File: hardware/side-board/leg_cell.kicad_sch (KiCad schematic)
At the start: 63 parts, among them IC201 STM32C092KCT6, IC202 TCAN332DR, IC203 TPS56A37RPAR, IC204 INA181A1IDBVR, J201 Servo Connector, J202 Servo Connector, J203 Servo Connector, J204 TC2050, J205 Conn_01x06

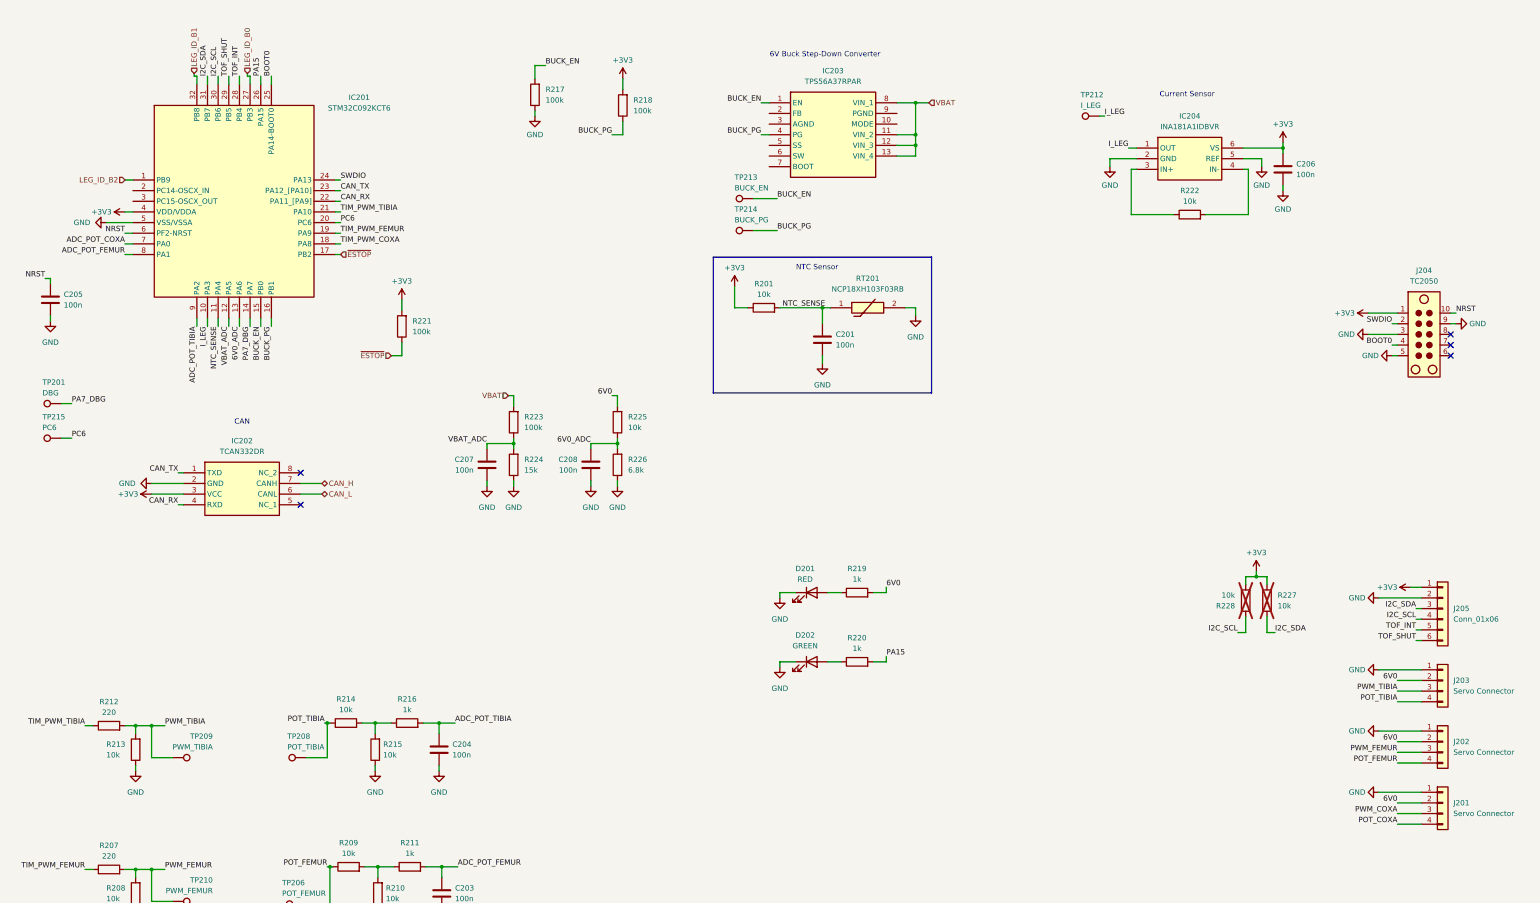
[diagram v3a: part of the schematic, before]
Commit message: Updated schematic for leg
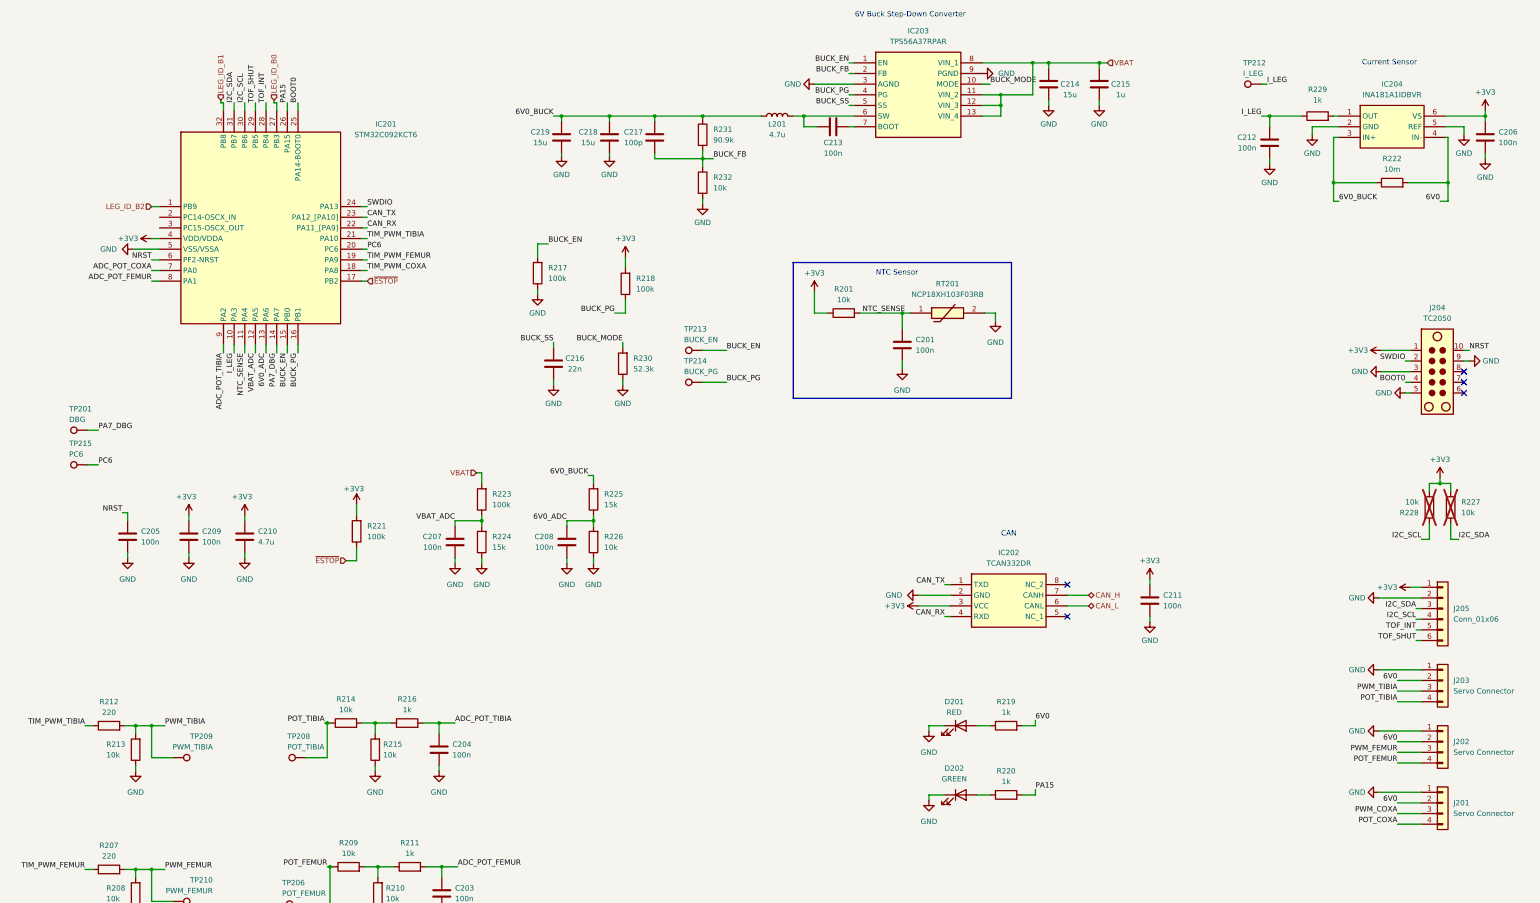
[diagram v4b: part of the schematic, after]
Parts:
- added C209, C211, C212, C213: 100n, Capacitor_SMD:C_0805_2012Metric, symbol Device:C
- added C210: 4.7u, Capacitor_SMD:C_0805_2012Metric, symbol Device:C
- added C214, C218, C219: 15u, Capacitor_SMD:C_0805_2012Metric, symbol Device:C
- added C215: 1u, Capacitor_SMD:C_0805_2012Metric, symbol Device:C
- added C216: 22n, Capacitor_SMD:C_0805_2012Metric, symbol Device:C
- added C217: 100p, Capacitor_SMD:C_0805_2012Metric, symbol Device:C
- added L201: 4.7u, symbol Device:L
- added R229: 1k, Resistor_SMD:R_0603_1608Metric, symbol Device:R
- added R230: 52.3k, Resistor_SMD:R_0603_1608Metric, symbol Device:R
- added R231: 90.9k, Resistor_SMD:R_0805_2012Metric, symbol Device:R
- added R232: 10k, Resistor_SMD:R_0805_2012Metric, symbol Device:R
- R222: value 10k -> 10m; footprint Resistor_SMD:R_0603_1608Metric -> Resistor_SMD:R_2512_6332Metric
- R225: value 10k -> 15k
- R226: value 6.8k -> 10k
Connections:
- net +3V3: now also C209.2, C210.2, C211.2
- net 6V0: now also IC204.4 (IN-), R222.2; no longer R225.2
- net GND: now also IC203.3 (AGND), IC203.9 (PGND), C209.1, C210.1, C211.1, C212.2, C214.2, C215.2, C216.2, C218.1, C219.1, R230.1, R232.2
- net I_LEG: now also C212.1, R229.1; no longer IC204.1 (OUT)
- net VBAT: now also C214.1, C215.1
- net 6V0_BUCK: now reaches IC204.3 (IN+), R222.1
- net 6V0_BUCK: now also R225.2, C217.2, C218.2, C219.2, L201.1, R231.1
- net BUCK_MODE: now reaches IC203.10 (MODE)
- net BUCK_MODE: now also R230.2
- net BUCK_FB: now reaches IC203.2 (FB)
- net BUCK_FB: now also C217.1, R231.2, R232.1
- net BUCK_SS: now reaches IC203.5 (SS)
- net BUCK_SS: now also C216.1
- net at IC203.6 (SW): now also C213.2, L201.2
- net at IC203.7 (BOOT): now also C213.1
- new net: IC204.1 (OUT), R229.2
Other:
- moved on the sheet: C201, C205, C206, C207, C208, D201, D202, IC201, IC202, IC203, IC204, J204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

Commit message: Updated side board schematic
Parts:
- added C220, C221: 10p, Capacitor_SMD:C_0805_2012Metric, symbol Device:C
- added Y201: Crystal_GND24, Crystal:Crystal_SMD_2016-4Pin_2.0x1.6mm, symbol Device:Crystal_GND24
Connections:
- net GND: now also C220.1, C221.1, Y201.2 (G), Y201.4 (G)
- net OSC_IN: now reaches IC201.2 (PC14-OSCX_IN)
- net OSC_IN: now also C221.2, Y201.3
- net OSC_OUT: now reaches IC201.3 (PC15-OSCX_OUT)
- net OSC_OUT: now also C220.2, Y201.1
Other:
- note added: "Configs"
- moved on the sheet: C201, C205, C206, C207, C208, C209, C210, C212, C213, C214, C215, C216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

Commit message: Segregated specific libs into shared libs
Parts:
- IC201: footprint side-board:QFP80P900X900X160-32N -> vector:QFP80P900X900X160-32N; symbol side-board:STM32C092KCT6 -> vector:STM32C092KCT6
- IC202: footprint side-board:SOIC127P600X175-8N -> vector:SOIC127P600X175-8N; symbol side-board:TCAN332DR -> vector:TCAN332DR
- RT201: footprint side-board:THRMC1608X95N -> vector:THRMC1608X95N; symbol side-board:NCP18XH103F03RB -> vector:NCP18XH103F03RB
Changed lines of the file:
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@@
 	)
 	(symbol
-		(lib_id "side-board:TCAN332DR")
+		(lib_id "vector:TCAN332DR")
 		(at 244.475 154.94 0)
 		(unit 1)
@@
 			)
 		)
-		(property "Footprint" "side-board:SOIC127P600X175-8N"
+		(property "Footprint" "vector:SOIC127P600X175-8N"
 			(at 268.605 249.86 0)
 			(hide yes)
@@
 	)
 	(symbol
-		(lib_id "side-board:NCP18XH103F03RB")
+		(lib_id "vector:NCP18XH103F03RB")
 		(at 238.76 92.71 0)
 		(unit 1)
@@
 			)
 		)
-		(property "Footprint" "side-board:THRMC1608X95N"
+		(property "Footprint" "vector:THRMC1608X95N"
 			(at 252.73 188.9 0)
 			(hide yes)
@@
 	)
 	(symbol
-		(lib_id "side-board:STM32C092KCT6")
+		(lib_id "vector:STM32C092KCT6")
 		(at 50.8 62.23 0)
 		(unit 1)
@@
 			)
 		)
-		(property "Footprint" "side-board:QFP80P900X900X160-32N"
+		(property "Footprint" "vector:QFP80P900X900X160-32N"
 			(at 95.25 141.91 0)
 			(hide yes)

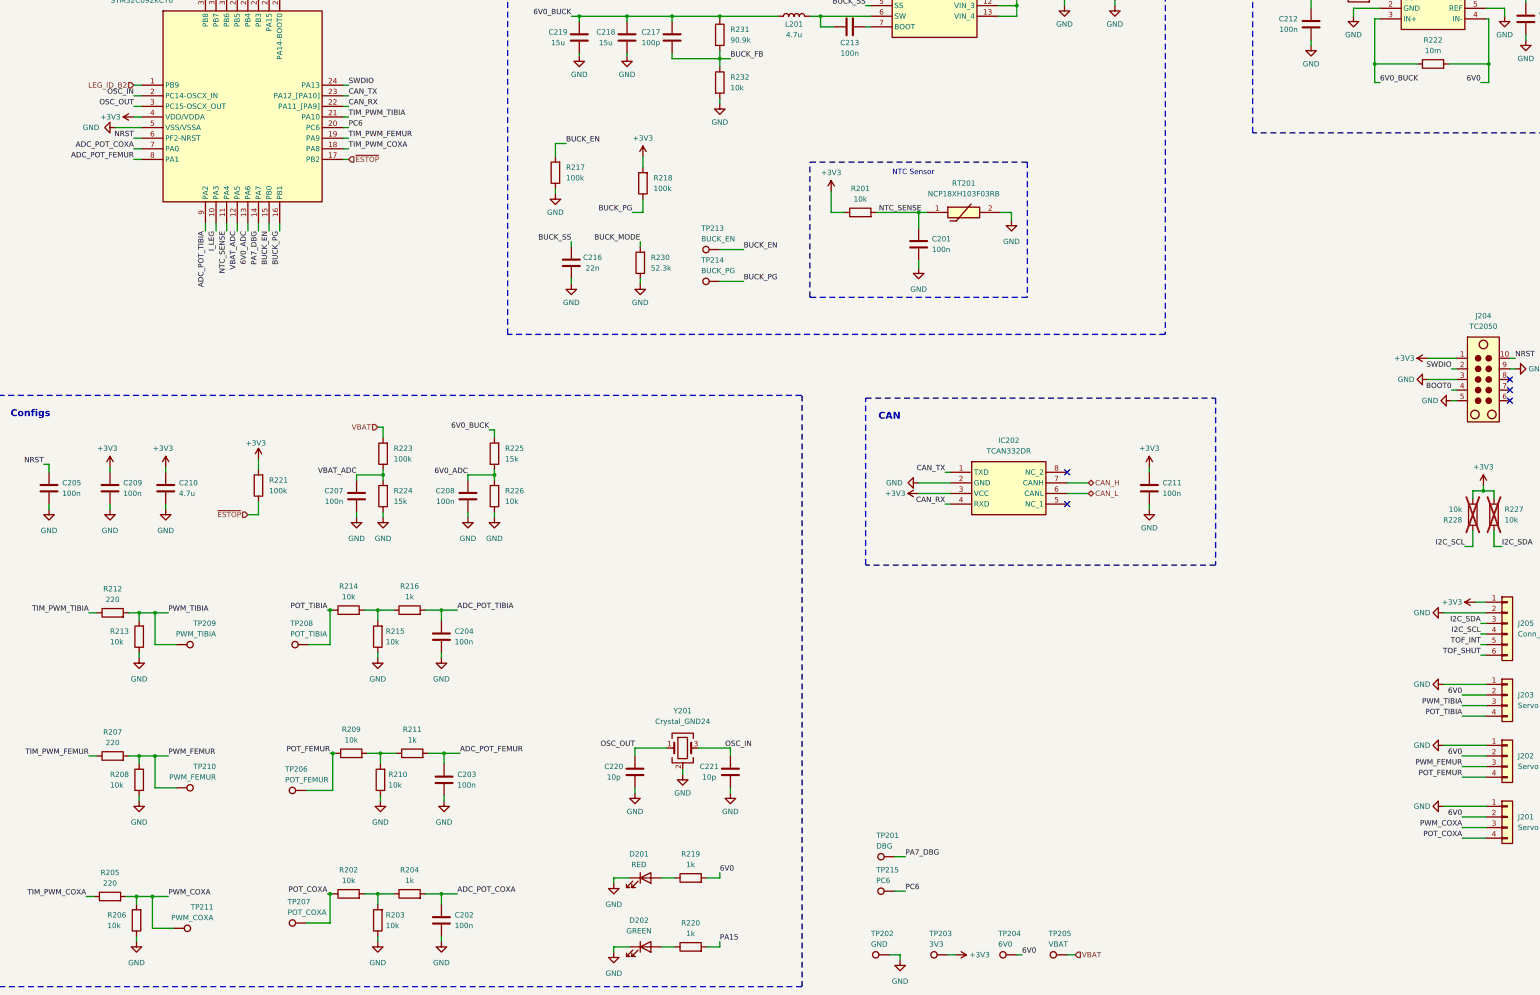
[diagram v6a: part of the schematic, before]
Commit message: Added more ICs for power board
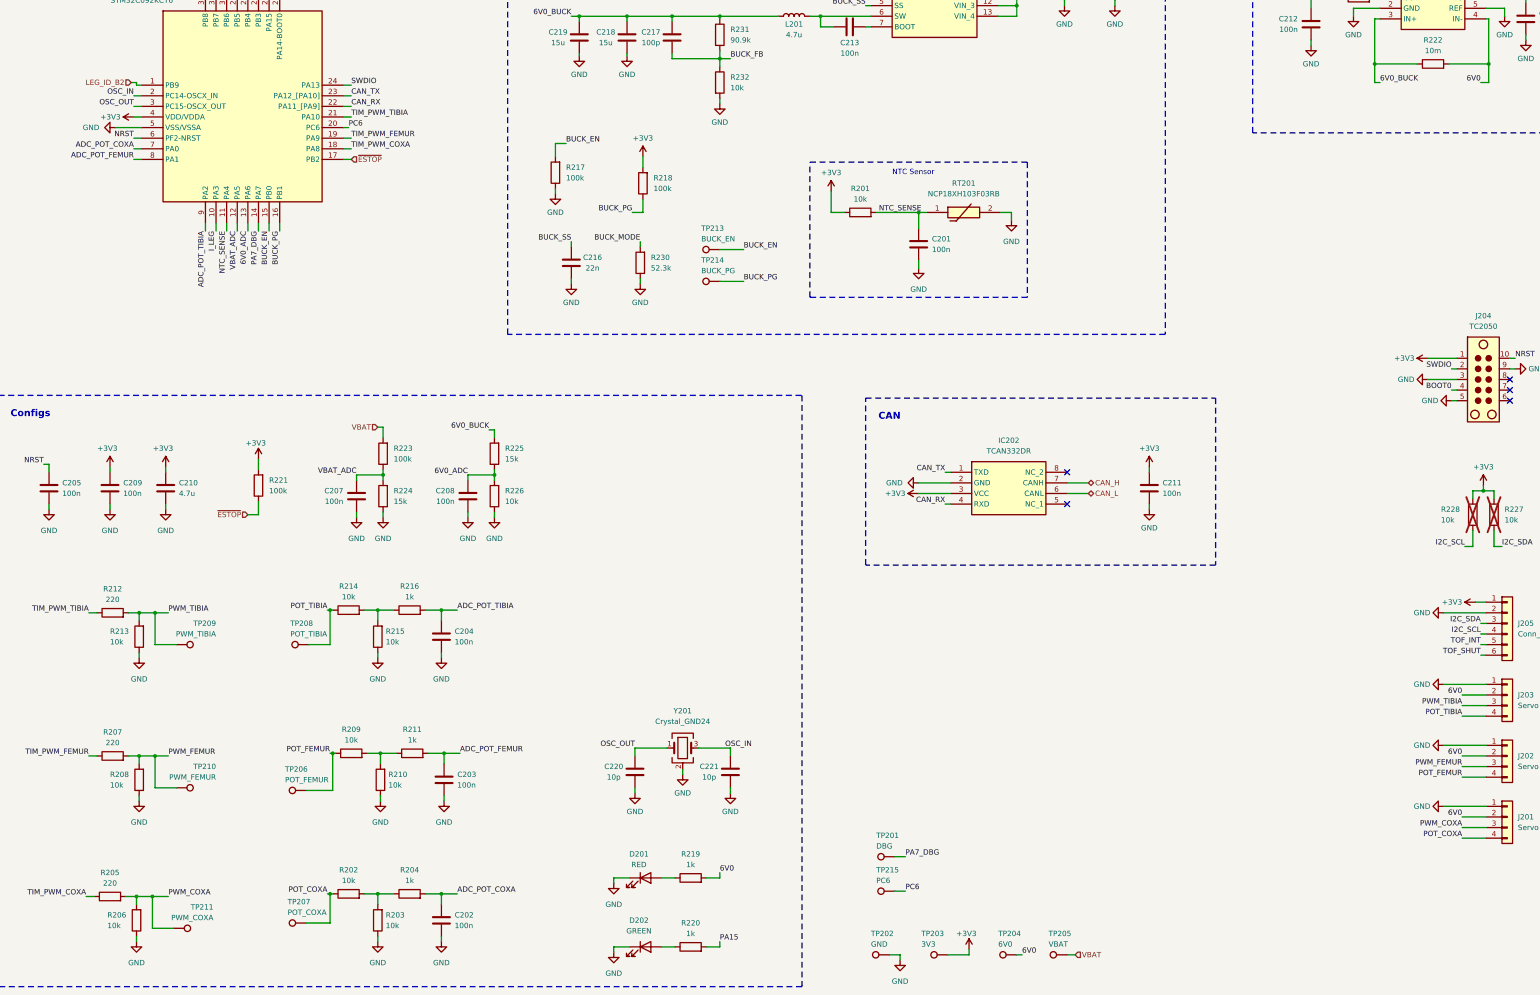
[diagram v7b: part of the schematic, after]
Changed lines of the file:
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@@
 	(wire
 		(pts
-			(xy 48.895 62.23) (xy 50.8 62.23)
+			(xy 48.26 61.595) (xy 49.53 61.595)
 		)
 		(stroke
@@
 	(wire
 		(pts
-			(xy 100.33 67.31) (xy 99.06 67.31)
+			(xy 100.965 67.31) (xy 99.06 67.31)
 		)
 		(stroke
@@
 	(wire
 		(pts
-			(xy 100.33 64.77) (xy 99.06 64.77)
+			(xy 100.965 64.77) (xy 99.06 64.77)
 		)
 		(stroke
@@
 	(wire
 		(pts
-			(xy 100.33 62.23) (xy 99.06 62.23)
+			(xy 100.965 62.23) (xy 99.06 62.23)
 		)
 		(stroke
@@
 	(wire
 		(pts
-			(xy 100.33 74.93) (xy 99.06 74.93)
+			(xy 100.965 74.93) (xy 99.06 74.93)
 		)
 		(stroke
@@
 	(wire
 		(pts
+			(xy 49.53 62.23) (xy 50.8 62.23)
+		)
+		(stroke
+			(width 0)
+			(type default)
+		)
+	)
+	(wire
+		(pts
 			(xy 78.74 37.465) (xy 78.74 39.37)
 		)
@@
 	(wire
 		(pts
+			(xy 49.53 61.595) (xy 49.53 62.23)
+		)
+		(stroke
+			(width 0)
+			(type default)
+		)
+	)
+	(wire
+		(pts
 			(xy 177.8 45.72) (xy 189.23 45.72)
 		)
@@
 	(wire
 		(pts
-			(xy 100.33 77.47) (xy 99.06 77.47)
+			(xy 100.965 77.47) (xy 99.06 77.47)
 		)
 		(stroke
@@
 	(wire
 		(pts
-			(xy 243.84 270.51) (xy 245.745 270.51)
-		)
-		(stroke
-			(width 0)
-			(type default)
-		)
-	)
-	(wire
-		(pts
 			(xy 59.055 230.505) (xy 53.975 230.505)
 		)
@@
 	(wire
 		(pts
-			(xy 100.33 69.85) (xy 99.06 69.85)
+			(xy 100.965 69.85) (xy 99.06 69.85)
 		)
 		(stroke
@@
 	(wire
 		(pts
+			(xy 248.92 269.24) (xy 248.92 270.51)
+		)
+		(stroke
+			(width 0)
+			(type default)
+		)
+	)
+	(wire
+		(pts
 			(xy 184.15 220.98) (xy 191.77 220.98)
 		)
@@
 	(wire
 		(pts
+			(xy 248.92 270.51) (xy 243.84 270.51)
+		)
+		(stroke
+			(width 0)
+			(type default)
+		)
+	)
+	(wire
+		(pts
 			(xy 27.305 153.035) (xy 28.575 153.035)
 		)
@@
 	(wire
 		(pts
-			(xy 99.06 80.01) (xy 100.33 80.01)
+			(xy 99.06 80.01) (xy 100.965 80.01)
 		)
 		(stroke
@@
 	)
 	(label "CAN_RX"
-		(at 100.33 67.31 0)
+		(at 100.965 67.31 0)
 		(effects
 			(font
@@
 	)
 	(label "CAN_TX"
-		(at 100.33 64.77 0)
+		(at 100.965 64.77 0)
 		(effects
 			(font
@@
 	)
 	(label "TIM_PWM_TIBIA"
-		(at 100.33 69.85 0)
+		(at 100.965 69.85 0)
 		(effects
 			(font
@@
 	)
 	(label "TIM_PWM_COXA"
-		(at 100.33 77.47 0)
+		(at 100.965 77.47 0)
 		(effects
 			(font
@@
 	)
 	(label "SWDIO"
-		(at 100.33 62.23 0)
+		(at 100.965 62.23 0)
 		(effects
 			(font
@@
 	)
 	(label "TIM_PWM_FEMUR"
-		(at 100.33 74.93 0)
+		(at 100.965 74.93 0)
 		(effects
 			(font
@@
 	(hierarchical_label "LEG_ID_B2"
 		(shape input)
-		(at 48.895 62.23 180)
+		(at 48.26 61.595 180)
 		(effects
 			(font
@@
 	(hierarchical_label "~{ESTOP}"
 		(shape input)
-		(at 100.33 80.01 0)
+		(at 100.965 80.01 0)
 		(effects
 			(font
@@
 		(dnp no)
 		(property "Reference" "TP203"
-			(at 239.395 265.43 90)
+			(at 237.49 265.43 90)
 			(show_name no)
 			(do_not_autoplace no)
@@
 		)
 		(property "Value" "3V3"
-			(at 239.395 267.97 90)
+			(at 237.49 267.97 90)
 			(show_name no)
 			(do_not_autoplace no)
@@
 		(dnp yes)
 		(property "Reference" "R228"
-			(at 367.03 166.37 0)
+			(at 361.95 163.83 0)
 			(show_name no)
 			(do_not_autoplace no)
@@
 					(size 1.27 1.27)
 				)
-				(justify right)
+				(justify left)
 			)
 		)
 		(property "Value" "10k"
-			(at 367.03 163.83 0)
+			(at 361.95 166.37 0)
 			(show_name no)
 			(do_not_autoplace no)
@@
 					(size 1.27 1.27)
 				)
-				(justify right)
+				(justify left)
 			)
 		)
@@
 	(symbol
 		(lib_id "power:+3V3")
-		(at 245.745 270.51 270)
+		(at 248.92 269.24 0)
 		(unit 1)
 		(body_style 1)
@@
 		(dnp no)
 		(property "Reference" "#PWR0221"
-			(at 241.935 270.51 0)
+			(at 248.92 273.05 0)
 			(hide yes)
 			(show_name no)
@@
 		)
 		(property "Value" "+3V3"
-			(at 251.46 270.51 90)
+			(at 248.285 265.43 0)
 			(show_name no)
 			(do_not_autoplace no)
@@
 		)
 		(property "Footprint" ""
-			(at 245.745 270.51 0)
+			(at 248.92 269.24 0)
 			(hide yes)
 			(show_name no)
@@
 		)
 		(property "Datasheet" ""
-			(at 245.745 270.51 0)
+			(at 248.92 269.24 0)
 			(hide yes)
 			(show_name no)
@@
 		)
 		(property "Description" "Power symbol creates a global label with name \"+3V3\""
-			(at 245.745 270.51 0)
+			(at 248.92 269.24 0)
 			(hide yes)
 			(show_name no)

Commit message: add side board e-stop diode, cell fuse and connectors
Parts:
- added D203: BAT54J, Diode_SMD:D_SOD-323F, symbol Device:D_Schottky
- added F201: 5A, symbol Device:Fuse
- added R233: 1k, Resistor_SMD:R_0603_1608Metric, symbol Device:R
- R203, R210, R215: now not fitted
- R204, R211, R216: value 1k -> 0
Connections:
- net BUCK_EN: now also D203.2 (A), R233.2; no longer IC201.15 (PB0)
- net VBAT: now also F201.1; no longer C214.1, C215.1, IC203.11 (VIN_2), IC203.12 (VIN_3), IC203.13 (VIN_4), IC203.8 (VIN_1)
- net ~{ESTOP}: now also D203.1 (K)
- new net MCU_BUCK_EN: IC201.15 (PB0), R233.1
- new net VBAT_F: C214.1, C215.1, F201.2, IC203.11 (VIN_2), IC203.12 (VIN_3), IC203.13 (VIN_4), IC203.8 (VIN_1)
